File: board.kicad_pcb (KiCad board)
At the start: 2 copper layers, 149 parts, among them SW1 5.2x5.2mm, U1 ATmega32U4-AU, Y1 16MHz

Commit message: PCB layout first pass
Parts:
- removed K_RFN1: MX-1.25U, MX_Alps_Hybrid:MXOnly-1.25U-NoLED
- added K_FN1: MX-1.25U, MX_Alps_Hybrid:MXOnly-1.25U-NoLED, F.Cu at (269.1, 149.2)
- K_DELETE1, K_INSERT1: value MX-2U -> MX-1U; footprint MX_Alps_Hybrid:MXOnly-2U-NoLED -> MX_Alps_Hybrid:MXOnly-1U-NoLED
- K_RSHIFT1: value MX-2.75U -> MX-2.25U; footprint MX_Alps_Hybrid:MXOnly-2.75U-NoLED -> MX_Alps_Hybrid:MXOnly-2.25U-NoLED
- K_\1: footprint MX_Alps_Hybrid:MXOnly-1U-NoLED -> MX_Alps_Hybrid:MXOnly-1.5U-NoLED
- moved SW1 330.1 mm to (352.4, 130.7), turned to 90 degrees
- moved USB1 318.7 mm to (338.1, 71.2)
- moved D30 307.9 mm to (360.4, 92.1), turned to 90 degrees
- moved D56 301.0 mm to (341.3, 130.2), turned to 90 degrees
- moved D15 287.3 mm to (360.4, 73.0), turned to 90 degrees
- moved D66 280.7 mm to (360.4, 149.2), turned to 90 degrees
- moved K_DELETE1 275.4 mm to (352.4, 92.1)
- moved K_BACK1 274.9 mm to (314.3, 73.0)
- moved K_RSHIFT1 267.1 mm to (302.4, 130.2)
- moved D65 266.6 mm to (341.3, 149.2), turned to 90 degrees
- moved D55 266.4 mm to (310.4, 130.2), turned to 90 degrees
- moved K_RCTRL1 261.2 mm to (292.9, 149.2)
- moved D43 259.6 mm to (319.9, 111.1), turned to 90 degrees
- moved K_UP1 256.1 mm to (333.4, 130.2)
- moved D63 254.5 mm to (300.8, 149.2), turned to 90 degrees
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
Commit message: Fixes
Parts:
- C1, C2, C3, C4, C5, C6, C7, D1, D10, D11, D12, D13, D14, D15, D16, D17, D18, D19, D2, D20, D21, D22, D23, D24, D25, D26, D27, D28, D29, D3, D30, D31, D32, D33, D34, D35, D36, D37, D38, D39, D4, D40, D41, D42, D43, D44, D45, D46, D47, D48, D49, D5, D50, D51, D52, D53, D54, D55, D56, D57, D58, D59, D6, D60, D61, D62, D63, D64, D65, D66, D7, D8, D9, R1, R2, R3, R4, R5, R6, U1, USB1, Y1: moved to B.Cu
- SW1: footprint random-keyboard-parts:Molex-0548190589 -> random-keyboard-parts:PushButton_6x6mm_TH_Pretty; moved to B.Cu
- moved C5 22.2 mm to (345.6, 100.2), turned to 180 degrees
- moved C4 20.5 mm to (342.3, 117.5), turned to 180 degrees
- moved C7 10.5 mm to (359.4, 114.7), turned to 90 degrees
- moved C2 10.3 mm to (339.1, 105.1)
- moved USB1 9.28 mm to (338.1, 62.0)
- moved C1 8.73 mm to (339.1, 114.6)
- moved R1 8.60 mm to (346.2, 120.3), turned to 270 degrees
- moved R6 7.01 mm to (334.7, 74.8)
- moved R5 6.93 mm to (341.6, 74.8)
- moved R2 6.13 mm to (356.9, 100.2)
- moved C6 5.37 mm to (359.4, 105.3), turned to 270 degrees
- moved R3 2.45 mm to (337.0, 74.8)
- moved R4 2.41 mm to (339.3, 74.8)
- moved Y1 0.94 mm to (339.1, 109.9), turned to 90 degrees
- moved U1 0.67 mm to (350.3, 110.0)
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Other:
- board outline added: 314.3 x 95.2 mm

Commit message: More fixes
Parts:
- SW1: footprint random-keyboard-parts:PushButton_6x6mm_TH_Pretty -> random-keyboard-parts:PushButton_6x6mm_TH
- moved R2 26.9 mm to (339.3, 120.7), turned to 0 degrees
- moved C6 25.0 mm to (336.8, 116.0), turned to 90 degrees
- moved C7 24.0 mm to (336.8, 106.6), turned to 270 degrees
- moved C5 21.1 mm to (350.6, 120.7), turned to 0 degrees
- moved C3 19.4 mm to (344.5, 101.6), turned to 180 degrees
- moved C1 18.1 mm to (357.1, 116.5)
- moved C2 18.1 mm to (357.1, 107.0)
- moved Y1 18.1 mm to (357.1, 111.8)
- moved C4 18.0 mm to (353.9, 103.8), turned to 0 degrees
- moved R6 6.99 mm to (341.7, 74.8)
- moved R5 6.97 mm to (334.6, 74.8)
- moved U1 4.56 mm to (345.9, 111.3), turned to 270 degrees
- moved R1 4.21 mm to (348.5, 123.8)
- moved R4 0.06 mm to (339.3, 74.8)

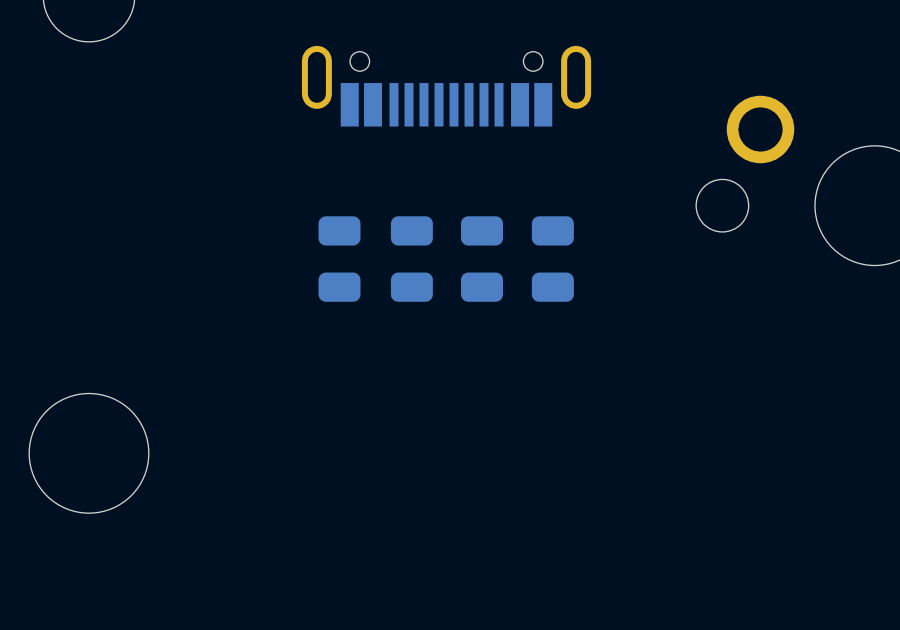
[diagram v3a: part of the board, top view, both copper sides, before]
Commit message: Fix ESD diode, ready to route
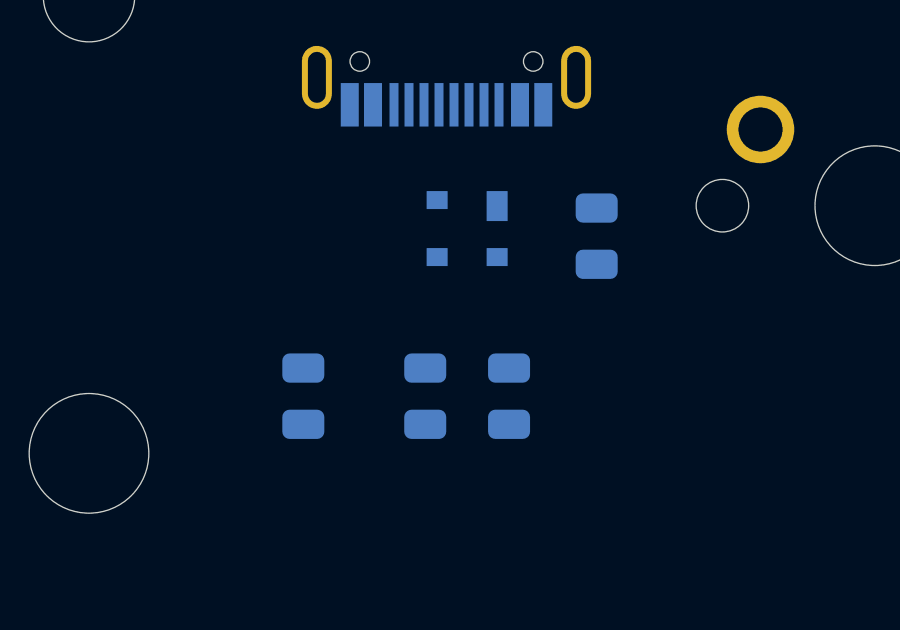
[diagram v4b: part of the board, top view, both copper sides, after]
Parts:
- added U2: PRTR5V0U2X, locallib:SOT143B, B.Cu at (338.8, 73.8)
- moved R5 4.73 mm to (333.4, 79.4)
- moved R4 4.66 mm to (340.2, 79.4)
- moved R3 4.59 mm to (337.4, 79.4)
- moved R6 1.65 mm to (343.2, 74.0)
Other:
- net class Power added: clearance 0.2, trace_width 0.375, via_dia 0.8, via_drill 0.4
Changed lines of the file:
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@@
     (tracks 0)
     (zones 0)
-    (modules 149)
+    (modules 150)
     (nets 130)
   )
@@
     (pad_drill 0.6)
     (pad_to_mask_clearance 0)
+    (solder_mask_min_width 0.25)
     (aux_axis_origin 0 0)
-    (visible_elements FFFFFF7F)
+    (visible_elements 7FFFFFFF)
     (pcbplotparams
       (layerselection 0x010fc_ffffffff)
@@
     (uvia_dia 0.3)
     (uvia_drill 0.1)
-    (add_net +5V)
     (add_net COL0)
     (add_net COL1)
@@
     (add_net D+)
     (add_net D-)
-    (add_net GND)
     (add_net "Net-(C1-Pad1)")
     (add_net "Net-(C2-Pad1)")
@@
     (add_net ROW3)
     (add_net ROW4)
+  )
+  (net_class Power ""
+    (clearance 0.2)
+    (trace_width 0.375)
+    (via_dia 0.8)
+    (via_drill 0.4)
+    (uvia_dia 0.3)
+    (uvia_drill 0.1)
+    (add_net +5V)
+    (add_net GND)
     (add_net VCC)
   )
@@
   )
   (module Resistor_SMD:R_0805_2012Metric (layer B.Cu)
-    (at 336.9945 74.803 90)
+    (at 337.439 79.375 90)
     (descr "Resistor SMD 0805 (2012 Metric), square (rectangular) end terminal, IPC_7351 nominal, (Body size source: https://docs.google.com/spreadsheets/d/1BsfQQcO9C6DZCsRaXUlFlo91Tg2WpOkGARC1WS5S8t0/edit?usp=sharing), generated with kicad-footprint-generator")
     (tags resistor)
@@
   )
   (module Resistor_SMD:R_0805_2012Metric (layer B.Cu)
-    (at 339.3313 74.803 90)
+    (at 340.233 79.375 90)
     (descr "Resistor SMD 0805 (2012 Metric), square (rectangular) end terminal, IPC_7351 nominal, (Body size source: https://docs.google.com/spreadsheets/d/1BsfQQcO9C6DZCsRaXUlFlo91Tg2WpOkGARC1WS5S8t0/edit?usp=sharing), generated with kicad-footprint-generator")
     (tags resistor)
@@
   )
   (module Resistor_SMD:R_0805_2012Metric (layer B.Cu)
-    (at 334.5815 74.803 90)
+    (at 333.375 79.375 90)
     (descr "Resistor SMD 0805 (2012 Metric), square (rectangular) end terminal, IPC_7351 nominal, (Body size source: https://docs.google.com/spreadsheets/d/1BsfQQcO9C6DZCsRaXUlFlo91Tg2WpOkGARC1WS5S8t0/edit?usp=sharing), generated with kicad-footprint-generator")
     (tags resistor)
@@
   )
   (module Resistor_SMD:R_0805_2012Metric (layer B.Cu)
-    (at 341.6935 74.803 90)
+    (at 343.154 74.041 90)
     (descr "Resistor SMD 0805 (2012 Metric), square (rectangular) end terminal, IPC_7351 nominal, (Body size source: https://docs.google.com/spreadsheets/d/1BsfQQcO9C6DZCsRaXUlFlo91Tg2WpOkGARC1WS5S8t0/edit?usp=sharing), generated with kicad-footprint-generator")
     (tags resistor)
@@
     )
   )
+  (module locallib:SOT143B (layer B.Cu)
+    (at 338.836 73.787 270)
+    (fp_text reference U2 (at 0 -2.45 270) (layer B.SilkS)
+      (effects (font (size 1 1) (thickness 0.15)) (justify mirror))
+    )
+    (fp_text value PRTR5V0U2X (at 0 2.3 270) (layer B.Fab)
+      (effects (font (size 1 1) (thickness 0.15)) (justify mirror))
+    )
+    (fp_line (start 0.55 1.45) (end 0.55 0.65) (layer B.Fab) (width 0.15))
+    (fp_line (start -0.55 0.65) (end -0.55 1.45) (layer B.Fab) (width 0.15))
+    (fp_line (start 0.55 -1.45) (end 0.55 -0.65) (layer B.Fab) (width 0.15))
+    (fp_line (start -0.1 -0.65) (end -0.1 -1.45) (layer B.Fab) (width 0.15))
+    (fp_line (start 1.45 -0.65) (end -1.45 -0.65) (layer B.Fab) (width 0.15))
+    (fp_line (start -1.45 0.65) (end 1.45 0.65) (layer B.Fab) (width 0.15))
+    (fp_line (start -1.45 -1.45) (end -1.45 1.45) (layer B.Fab) (width 0.15))
+    (fp_line (start 1.45 -1.45) (end -1.45 -1.45) (layer B.Fab) (width 0.15))
+    (fp_line (start 1.45 1.45) (end 1.45 -1.45) (layer B.Fab) (width 0.15))
+    (fp_line (start -1.45 1.45) (end 1.45 1.45) (layer B.Fab) (width 0.15))
+    (fp_line (start 1.45 -0.65) (end 1.45 0.65) (layer B.SilkS) (width 0.15))
+    (fp_line (start -1.45 -0.65) (end 1.45 -0.65) (layer B.SilkS) (width 0.15))
+    (fp_line (start -1.45 0.65) (end -1.45 -0.65) (layer B.SilkS) (width 0.15))
+    (fp_line (start -1.45 0.65) (end 1.45 0.65) (layer B.SilkS) (width 0.15))
+    (pad 3 smd rect (at 0.95 1 270) (size 0.6 0.7) (layers B.Cu B.Paste B.Mask)
+      (net 96 "Net-(R3-Pad2)"))
+    (pad 2 smd rect (at 0.95 -1 270) (size 0.6 0.7) (layers B.Cu B.Paste B.Mask)
+      (net 97 "Net-(R4-Pad2)"))
+    (pad 4 smd rect (at -0.95 1 270) (size 0.6 0.7) (layers B.Cu B.Paste B.Mask)
+      (net 129 VCC))
+    (pad 1 smd rect (at -0.75 -1 270) (size 1 0.7) (layers B.Cu B.Paste B.Mask)
+      (net 1 GND))
+  )
   (gr_line (start 359.56875 158.75) (end 50.00625 158.75) (layer Edge.Cuts) (width 0.2))

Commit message: Switches horizontal wiring
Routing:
- net ROW0: track 0.00 -> 313.2 mm
- net ROW1: track 0.00 -> 308.9 mm
- net ROW4: track 0.00 -> 304.6 mm
- net ROW3: track 0.00 -> 279.6 mm
- net ROW2: track 0.00 -> 263.3 mm
- net Net-(D53-Pad2): track 0.00 -> 6.87 mm
- net Net-(D15-Pad2): track 0.00 -> 6.87 mm
- net Net-(D43-Pad2): track 0.00 -> 6.87 mm
- net Net-(D42-Pad2): track 0.00 -> 6.87 mm
- net Net-(D30-Pad2): track 0.00 -> 6.87 mm
- net Net-(D27-Pad2): track 0.00 -> 6.87 mm
- net Net-(D26-Pad2): track 0.00 -> 6.87 mm
- net Net-(D66-Pad2): track 0.00 -> 6.87 mm
- net Net-(D63-Pad2): track 0.00 -> 6.87 mm
- net Net-(D62-Pad2): track 0.00 -> 6.87 mm
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
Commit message: Vertical routing
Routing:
- net COL10: track 0.00 -> 90.1 mm
- net COL11: track 0.00 -> 88.1 mm
- net COL6: track 0.00 -> 88.1 mm
- net COL2: track 0.00 -> 87.6 mm
- net COL12: track 0.00 -> 87.6 mm
- net COL1: track 0.00 -> 86.9 mm
- net COL0: track 0.00 -> 85.6 mm
- net COL13: track 0.00 -> 85.1 mm
- net COL7: track 0.00 -> 67.5 mm
- net COL9: track 0.00 -> 67.5 mm
- net COL4: track 0.00 -> 67.5 mm
- net COL8: track 0.00 -> 67.5 mm
- net COL5: track 0.00 -> 67.5 mm
- net COL3: track 0.00 -> 67.5 mm
- net COL15: track 0.00 -> 19.6 mm
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
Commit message: Route around USB, missing fuse
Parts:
- added F1: 500mA, Fuse:Fuse_1206_3216Metric, B.Cu at (333.2, 81.8)
- moved R5 3.27 mm to (330.2, 80.2)
- moved R6 1.44 mm to (343.9, 72.8)
- moved R3 0.89 mm to (336.6, 79.4)
- moved U2 0.70 mm to (338.1, 73.8)
- moved R4 0.51 mm to (339.7, 79.4)
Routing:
- net COL15: track 19.6 -> 86.5 mm
- net GND: track 0.00 -> 28.8 mm
- net VCC: track 0.00 -> 19.5 mm, vias 0 -> 2
- net Net-(R5-Pad2): track 0.00 -> 13.3 mm, vias 0 -> 2
- net Net-(R4-Pad2): track 0.00 -> 13.3 mm
- net Net-(R3-Pad2): track 0.00 -> 12.1 mm
- net Net-(R6-Pad2): track 0.00 -> 7.74 mm, vias 0 -> 2
- net ROW0: vias 0 -> 2
- added copper zone on B.Cu, net GND
